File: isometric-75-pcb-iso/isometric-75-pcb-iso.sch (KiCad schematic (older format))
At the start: 20 parts, among them J101 Conn_01x05, J102 Conn_01x06, Q101 AO3400A, SW101 SW_Push, U101 XC6206P332MR, U102 STM32F072CBTx

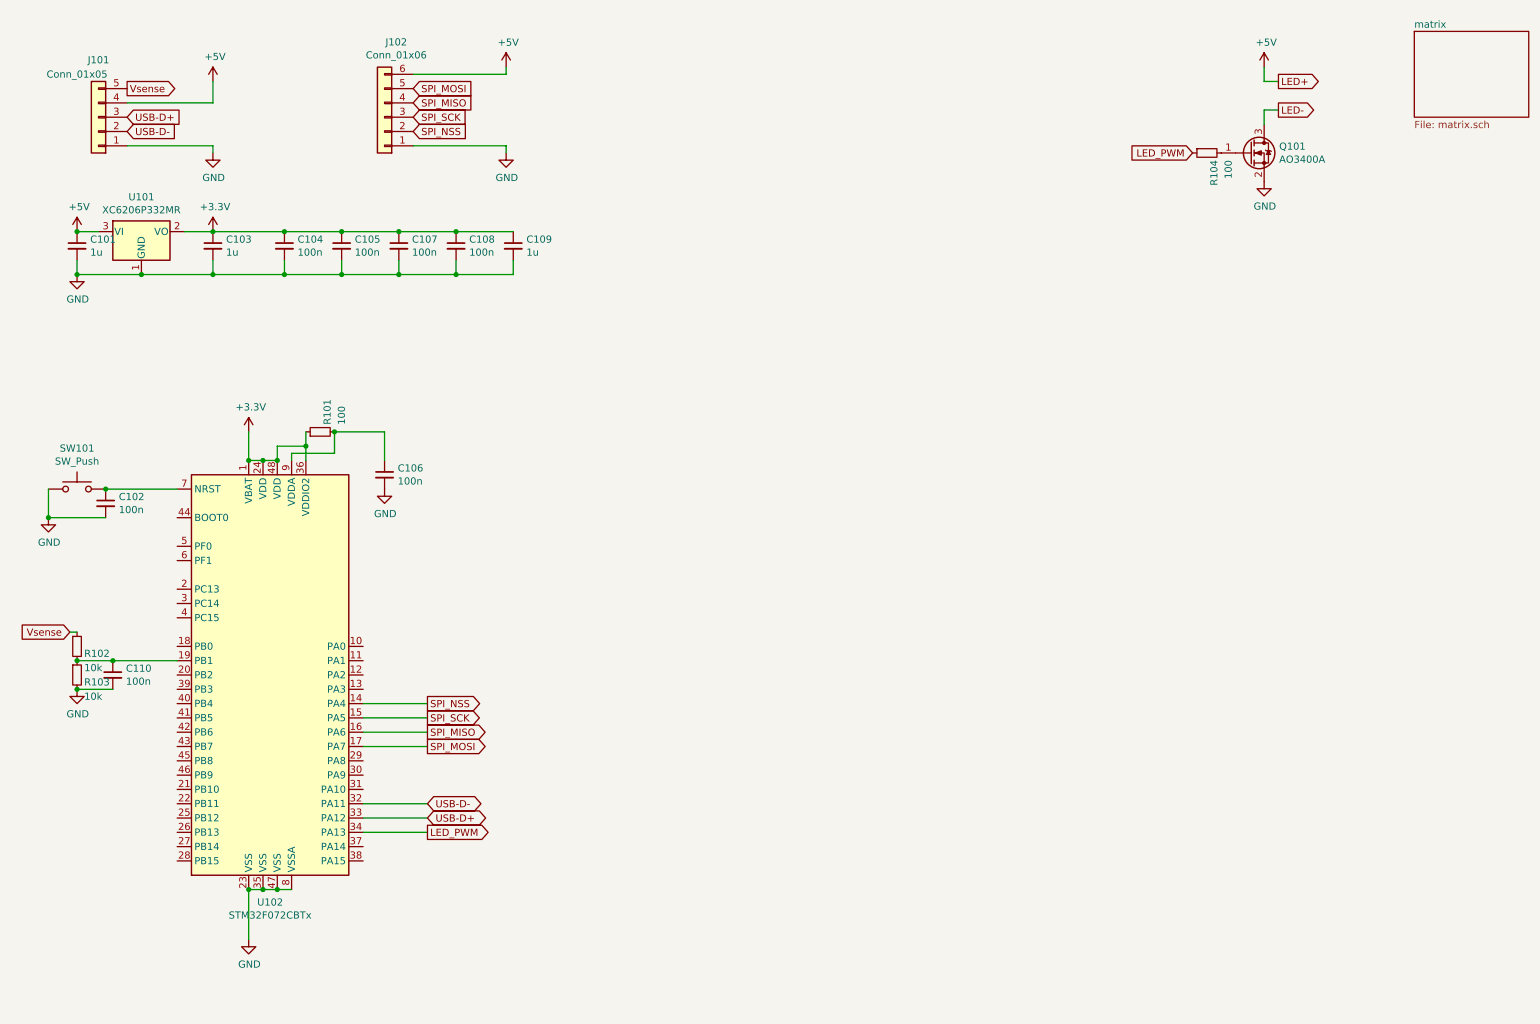
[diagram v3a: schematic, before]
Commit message: more pcb wiring
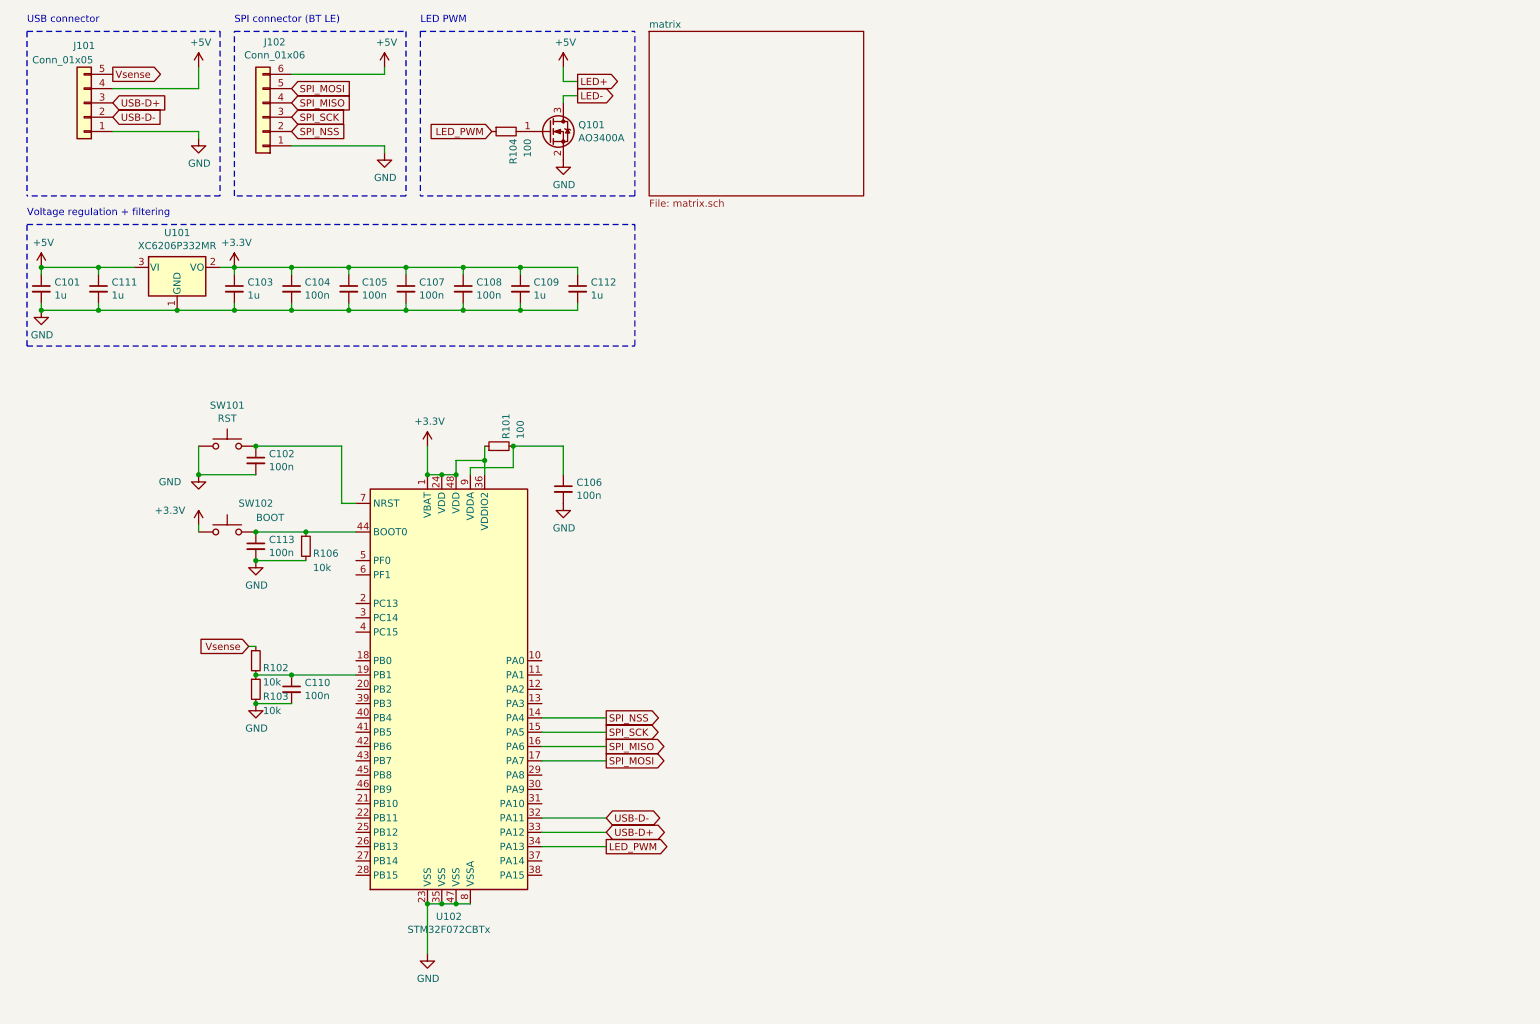
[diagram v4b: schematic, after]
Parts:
- added C111, C112: 1u, Capacitor_SMD:C_0603_1608Metric, symbol Device:C_Small
- added C113: 100n, Capacitor_SMD:C_0402_1005Metric, symbol Device:C_Small
- added R106: 10k, Resistor_SMD:R_0402_1005Metric, symbol Device:R_Small
- added SW102: BOOT, random-keyboard-parts:SKQG-1155865, symbol Switch:SW_Push
- C101, C103: footprint Capacitor_SMD:C_0402_1005Metric -> Capacitor_SMD:C_0603_1608Metric
- SW101: value SW_Push -> RST
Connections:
- net +3V3: now also C112.1, SW102.1
- net +5V: now also C111.1
- net GND: now also C111.2, C112.2, C113.2, R106.2
- net at U102.44 (BOOT0): now also C113.1, R106.1, SW102.2
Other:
- note added: "LED PWM"
- note added: "SPI connector (BT LE)"
- note added: "USB connector"
- note added: "Voltage regulation + filtering"
- moved on the sheet: C101, C102, C103, C104, C105, C106, C107, C108, C109, C110, J101, J102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

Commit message: connecting rows
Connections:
- net ROTB: now reaches U102.10 (PA0)
- net ROTA: now reaches U102.11 (PA1)
- net COL11: now reaches U102.13 (PA3)
- net COL12: now reaches U102.18 (PB0)
- net COL13: now reaches U102.20 (PB2)
- net COL14: now reaches U102.21 (PB10)
- net COL15: now reaches U102.22 (PB11)
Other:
- moved on the sheet: C110, R102, R103
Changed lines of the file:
@@
 L Device:C_Small C110
 U 1 1 5E7D4A32
-P 2400 5250
-F 0 "C110" H 2492 5296 50  0000 L CNN
-F 1 "100n" H 2492 5205 50  0000 L CNN
-F 2 "Capacitor_SMD:C_0402_1005Metric" H 2400 5250 50  0001 C CNN
-F 3 "~" H 2400 5250 50  0001 C CNN
-	1    2400 5250
+P 1200 5250
+F 0 "C110" H 1292 5296 50  0000 L CNN
+F 1 "100n" H 1292 5205 50  0000 L CNN
+F 2 "Capacitor_SMD:C_0402_1005Metric" H 1200 5250 50  0001 C CNN
+F 3 "~" H 1200 5250 50  0001 C CNN
+	1    1200 5250
 	1    0    0    -1
 $EndComp
@@
 L Device:R_Small R103
 U 1 1 5E7D5EC0
-P 2150 5250
-F 0 "R103" H 2200 5200 50  0000 L CNN
-F 1 "10k" H 2200 5100 50  0000 L CNN
-F 2 "Resistor_SMD:R_0402_1005Metric" H 2150 5250 50  0001 C CNN
-F 3 "~" H 2150 5250 50  0001 C CNN
-	1    2150 5250
+P 950 5250
+F 0 "R103" H 1000 5200 50  0000 L CNN
+F 1 "10k" H 1000 5100 50  0000 L CNN
+F 2 "Resistor_SMD:R_0402_1005Metric" H 950 5250 50  0001 C CNN
+F 3 "~" H 950 5250 50  0001 C CNN
+	1    950  5250
 	1    0    0    -1
 $EndComp
@@
 L Device:R_Small R102
 U 1 1 5E7D6E4F
-P 2150 5050
-F 0 "R102" H 2200 5000 50  0000 L CNN
-F 1 "10k" H 2200 4900 50  0000 L CNN
-F 2 "Resistor_SMD:R_0402_1005Metric" H 2150 5050 50  0001 C CNN
-F 3 "~" H 2150 5050 50  0001 C CNN
-	1    2150 5050
-	1    0    0    -1
-$EndComp
-Connection ~ 2150 5150
-Text GLabel 2100 4950 0    50   Input ~ 0
+P 950 5050
+F 0 "R102" H 1000 5000 50  0000 L CNN
+F 1 "10k" H 1000 4900 50  0000 L CNN
+F 2 "Resistor_SMD:R_0402_1005Metric" H 950 5050 50  0001 C CNN
+F 3 "~" H 950 5050 50  0001 C CNN
+	1    950  5050
+	1    0    0    -1
+$EndComp
+Connection ~ 950  5150
+Text GLabel 900  4950 0    50   Input ~ 0
 Vsense
 Wire Wire Line
-	2150 4950 2100 4950
+	950  4950 900  4950
 $Comp
 L power:GND #PWR0112
 U 1 1 5E7DB3B5
-P 2150 5350
-F 0 "#PWR0112" H 2150 5100 50  0001 C CNN
-F 1 "GND" H 2155 5177 50  0000 C CNN
-F 2 "" H 2150 5350 50  0001 C CNN
-F 3 "" H 2150 5350 50  0001 C CNN
-	1    2150 5350
-	1    0    0    -1
-$EndComp
-Connection ~ 2150 5350
-Connection ~ 2400 5150
-Wire Wire Line
-	2400 5150 2850 5150
-Wire Wire Line
-	2150 5150 2400 5150
-Wire Wire Line
-	2150 5350 2400 5350
+P 950 5350
+F 0 "#PWR0112" H 950 5100 50  0001 C CNN
+F 1 "GND" H 955 5177 50  0000 C CNN
+F 2 "" H 950 5350 50  0001 C CNN
+F 3 "" H 950 5350 50  0001 C CNN
+	1    950  5350
+	1    0    0    -1
+$EndComp
+Connection ~ 950  5350
+Wire Wire Line
+	950  5150 1200 5150
+Wire Wire Line
+	950  5350 1200 5350
 $Comp
 L Device:R_Small R104
@@
 Text GLabel 1150 950  2    50   Output ~ 0
 Vsense
-Text GLabel 1150 1150 2    50   Input ~ 0
+Text GLabel 1150 1150 2    50   BiDi ~ 0
 USB-D+
-Text GLabel 1150 1250 2    50   Input ~ 0
+Text GLabel 1150 1250 2    50   BiDi ~ 0
 USB-D-
 $Comp
@@
 	1    0    0    -1
 $EndComp
+Text GLabel 4600 5050 2    50   Input ~ 0
+ROTB
+Text GLabel 4600 5150 2    50   Input ~ 0
+ROTA
+Wire Wire Line
+	4150 5050 4600 5050
+Wire Wire Line
+	4150 5150 4600 5150
+Text GLabel 2500 6150 0    50   Input ~ 0
+COL15
+Text GLabel 2500 6050 0    50   Input ~ 0
+COL14
+Connection ~ 1200 5150
+Text GLabel 2500 5250 0    50   Input ~ 0
+COL13
+Wire Wire Line
+	1200 5150 2850 5150
+Wire Wire Line
+	2500 5250 2850 5250
+Wire Wire Line
+	2500 6050 2850 6050
+Wire Wire Line
+	2500 6150 2850 6150
+Text GLabel 2500 5050 0    50   Input ~ 0
+COL12
+Wire Wire Line
+	2500 5050 2850 5050
+Text GLabel 4600 5350 2    50   Input ~ 0
+COL11
+Wire Wire Line
+	4150 5350 4600 5350
 $EndSCHEMATC

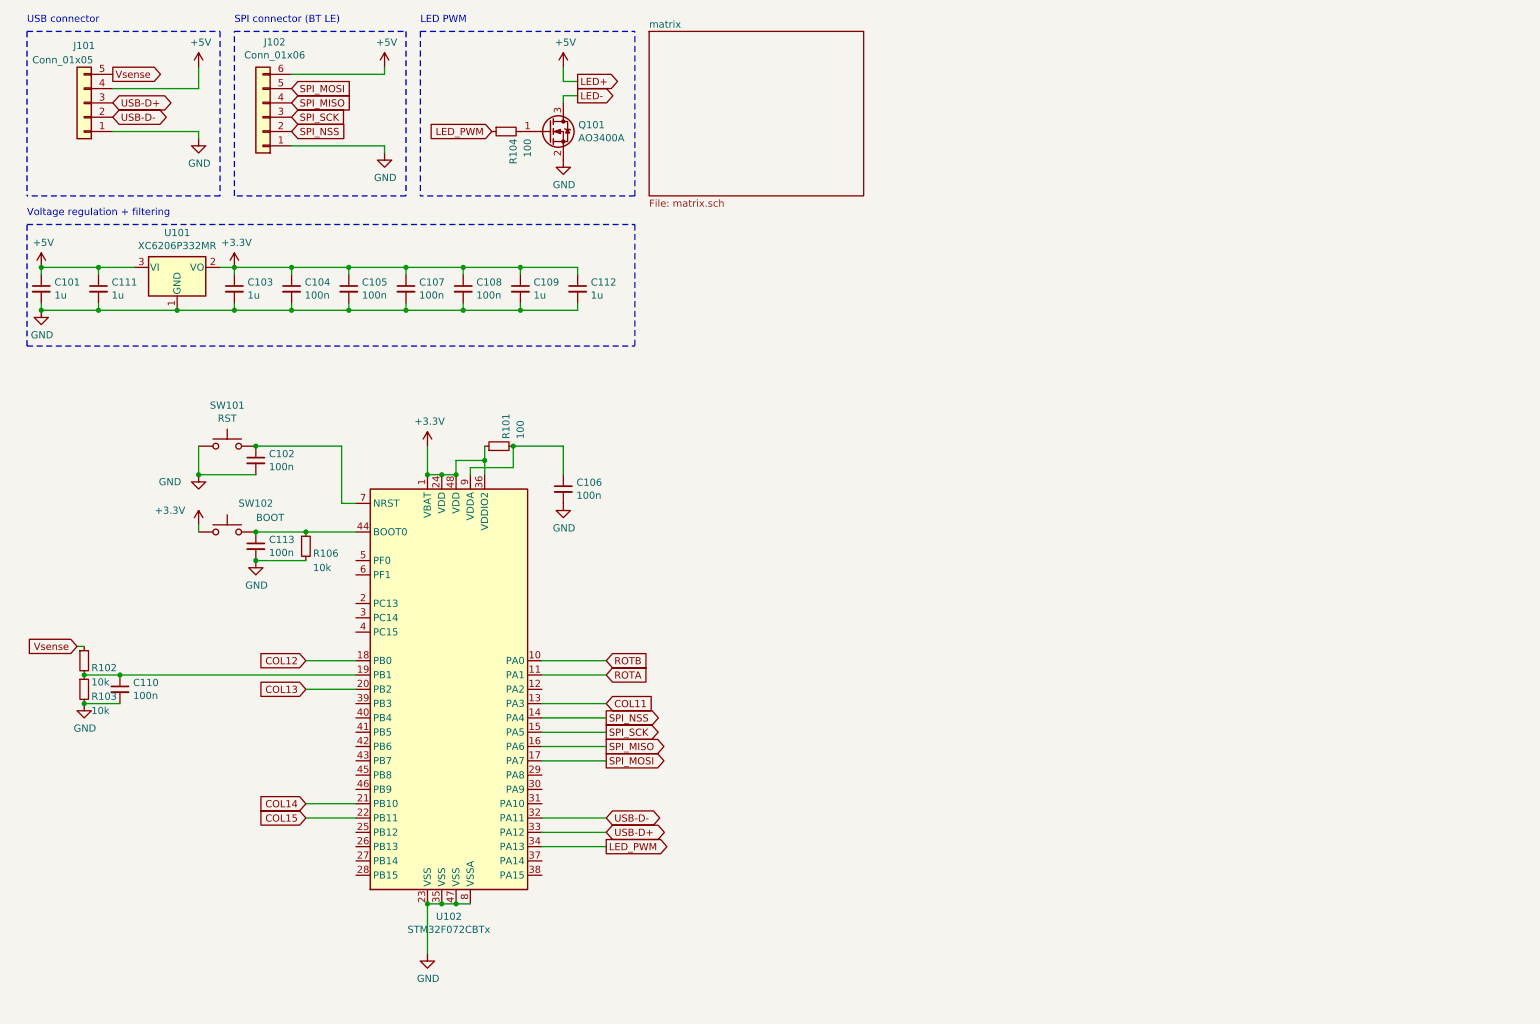
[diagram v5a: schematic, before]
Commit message: finished wiring cols, changed jlc connector color
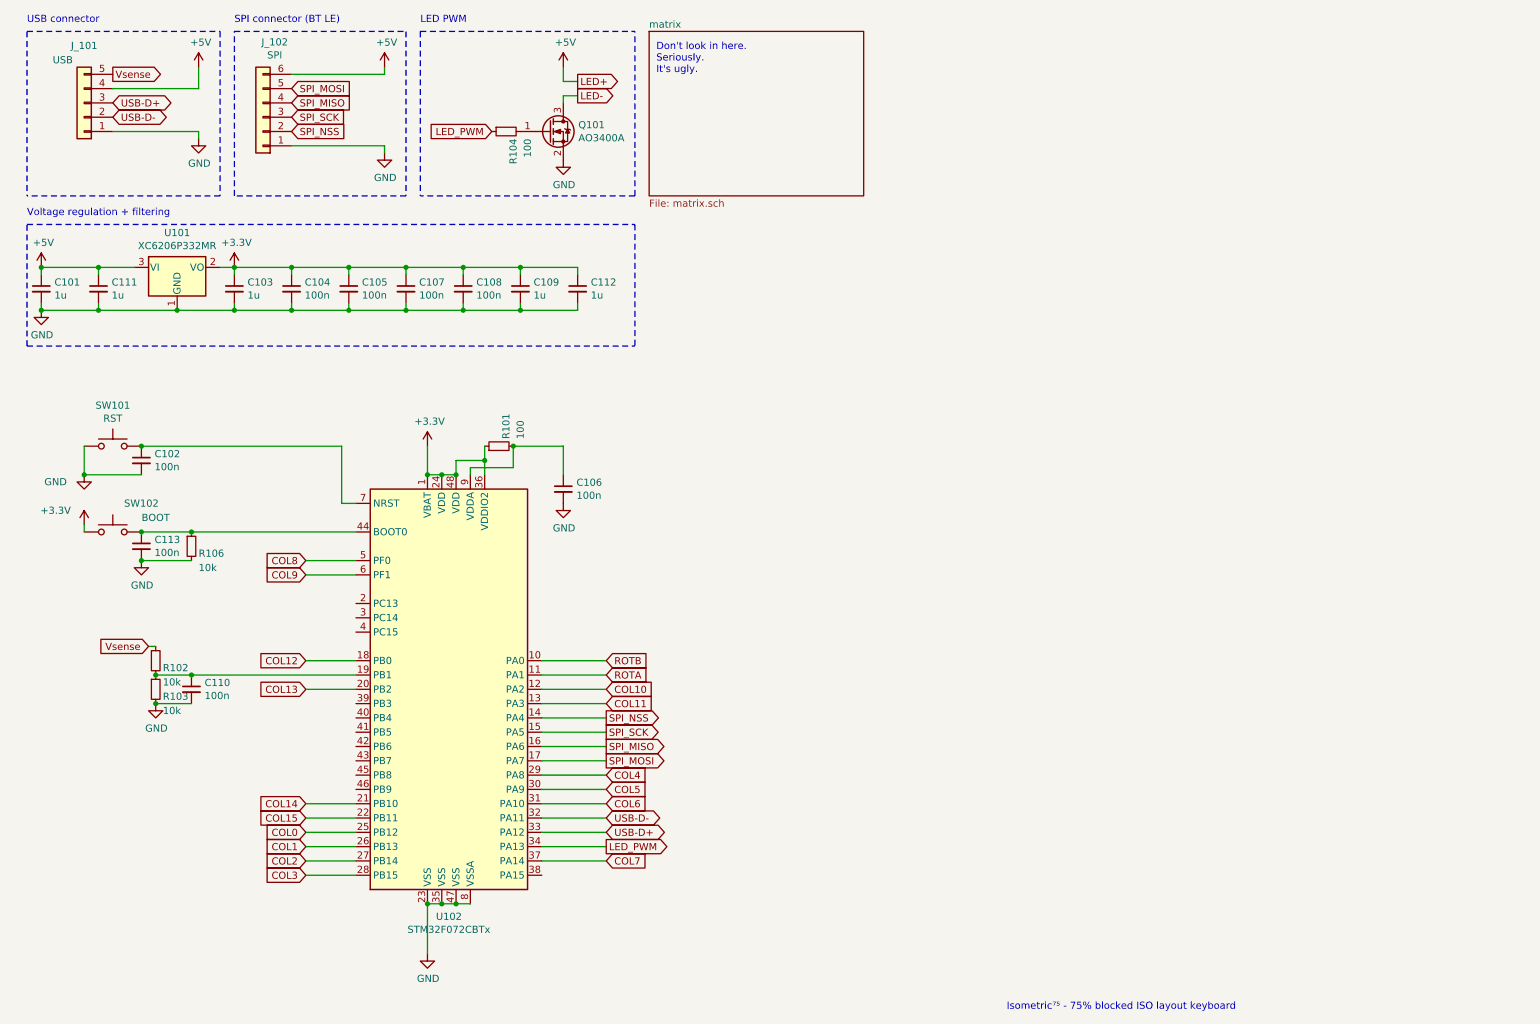
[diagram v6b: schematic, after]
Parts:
- J_101: renamed from J101; value Conn_01x05 -> USB
- J_102: renamed from J102; value Conn_01x06 -> SPI
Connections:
- net COL10: now reaches U102.12 (PA2)
- net COL0: now reaches U102.25 (PB12)
- net COL1: now reaches U102.26 (PB13)
- net COL2: now reaches U102.27 (PB14)
- net COL3: now reaches U102.28 (PB15)
- net COL4: now reaches U102.29 (PA8)
- net COL5: now reaches U102.30 (PA9)
- net COL6: now reaches U102.31 (PA10)
- net COL7: now reaches U102.37 (PA14)
- net COL8: now reaches U102.5 (PF0)
- net COL9: now reaches U102.6 (PF1)
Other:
- note added: "Don't look in here.\nSeriously. \nIt's ugly.\n"
- note added: "Isometric⁷⁵ - 75% blocked ISO layout keyboard"
- moved on the sheet: C102, C110, C113, R102, R103, R106, SW101, SW102
